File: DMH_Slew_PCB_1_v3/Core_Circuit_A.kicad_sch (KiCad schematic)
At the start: 60 parts, among them J1 TS_Jack_6.35mm_Sw, J11 Conn_02x03_Top_Bottom, J12 Conn_02x06_Top_Bottom, J13 Conn_02x03_Top_Bottom, J14 Conn_02x03_Top_Bottom, J15 Conn_02x06_Top_Bottom, J16 Conn_02x03_Top_Bottom, J17 Conn_01x08, J18 Conn_01x08, J19 Conn_01x08, J2 TS_Jack_6.35mm_Sw, J20 Conn_01x08, J3 TS_Jack_6.35mm_Sw, Q1 BC548, Q2 BC548, Q3 BC558, Q4 BC558, SW1 SW_DPDT_3way, SW2 SW_DPDT, SW3 SPDT_OnOffOn, U1 TL074, U2 TL074

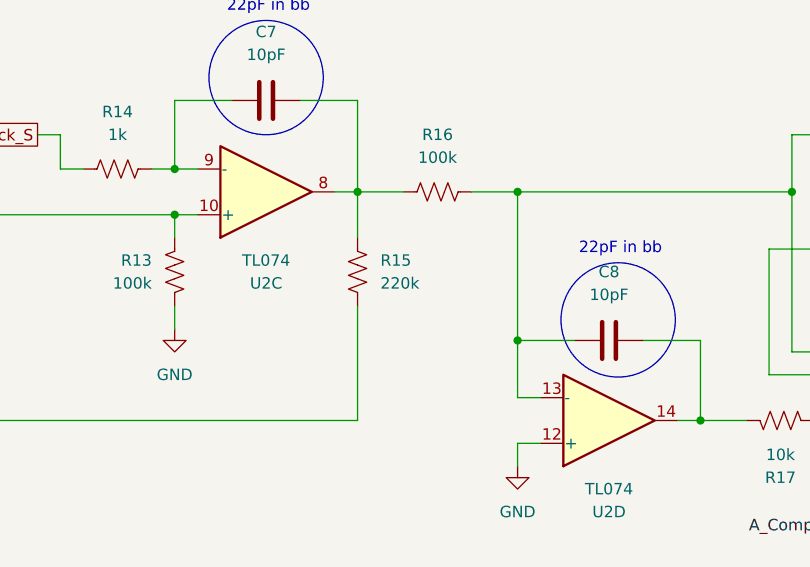
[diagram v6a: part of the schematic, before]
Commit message: Changed loopback resistor to 82k
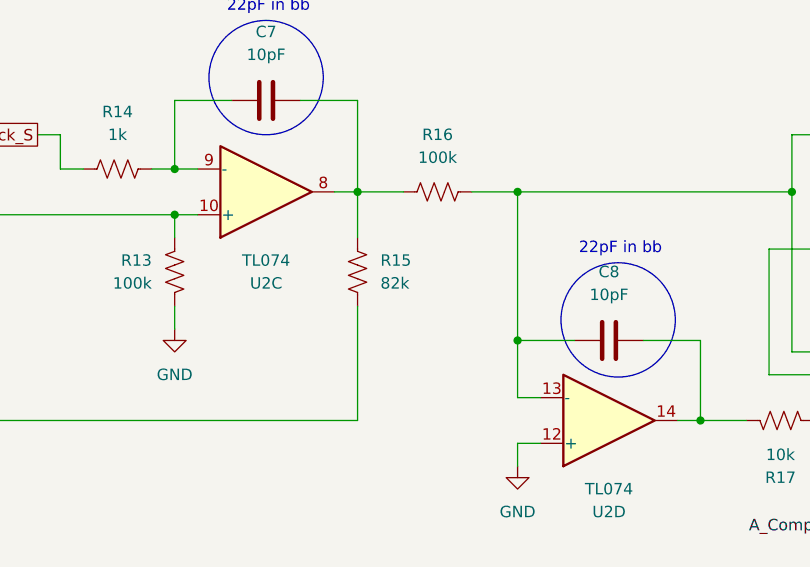
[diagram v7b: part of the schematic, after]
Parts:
- R15: value 220k -> 82k
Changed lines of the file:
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@@
 			)
 		)
-		(property "Value" "220k"
+		(property "Value" "82k"
 			(at 146.05 175.2599 0)
 			(effects

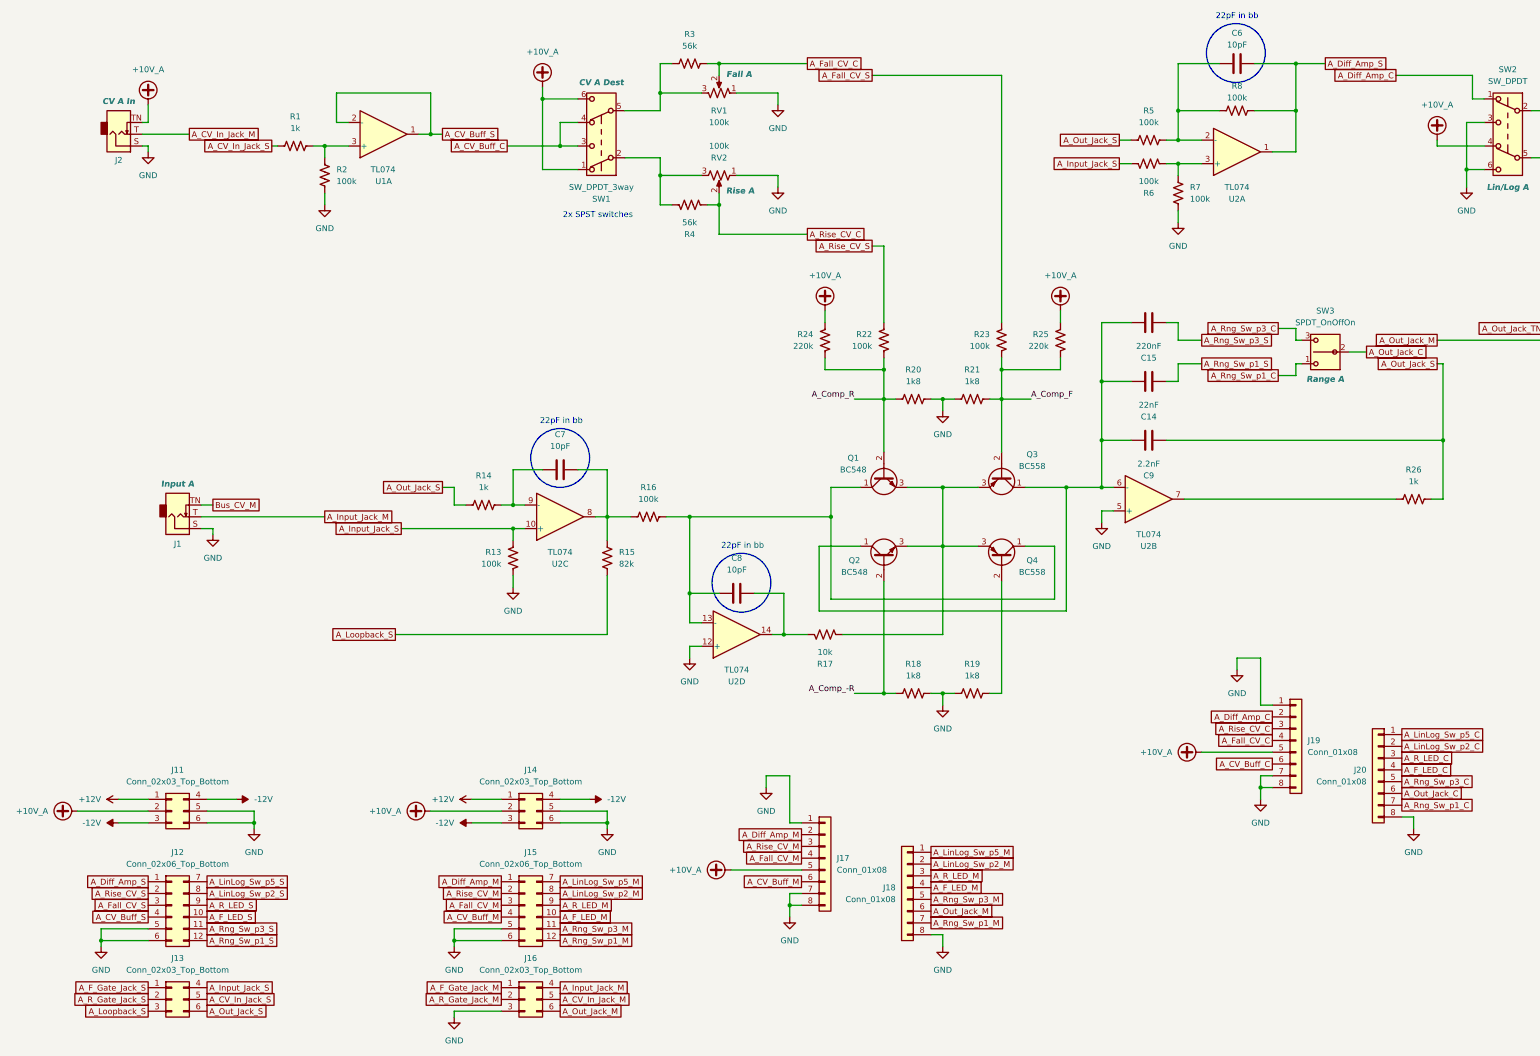
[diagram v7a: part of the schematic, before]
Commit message: Redesigned Main PCB
and regenerated Gerbers
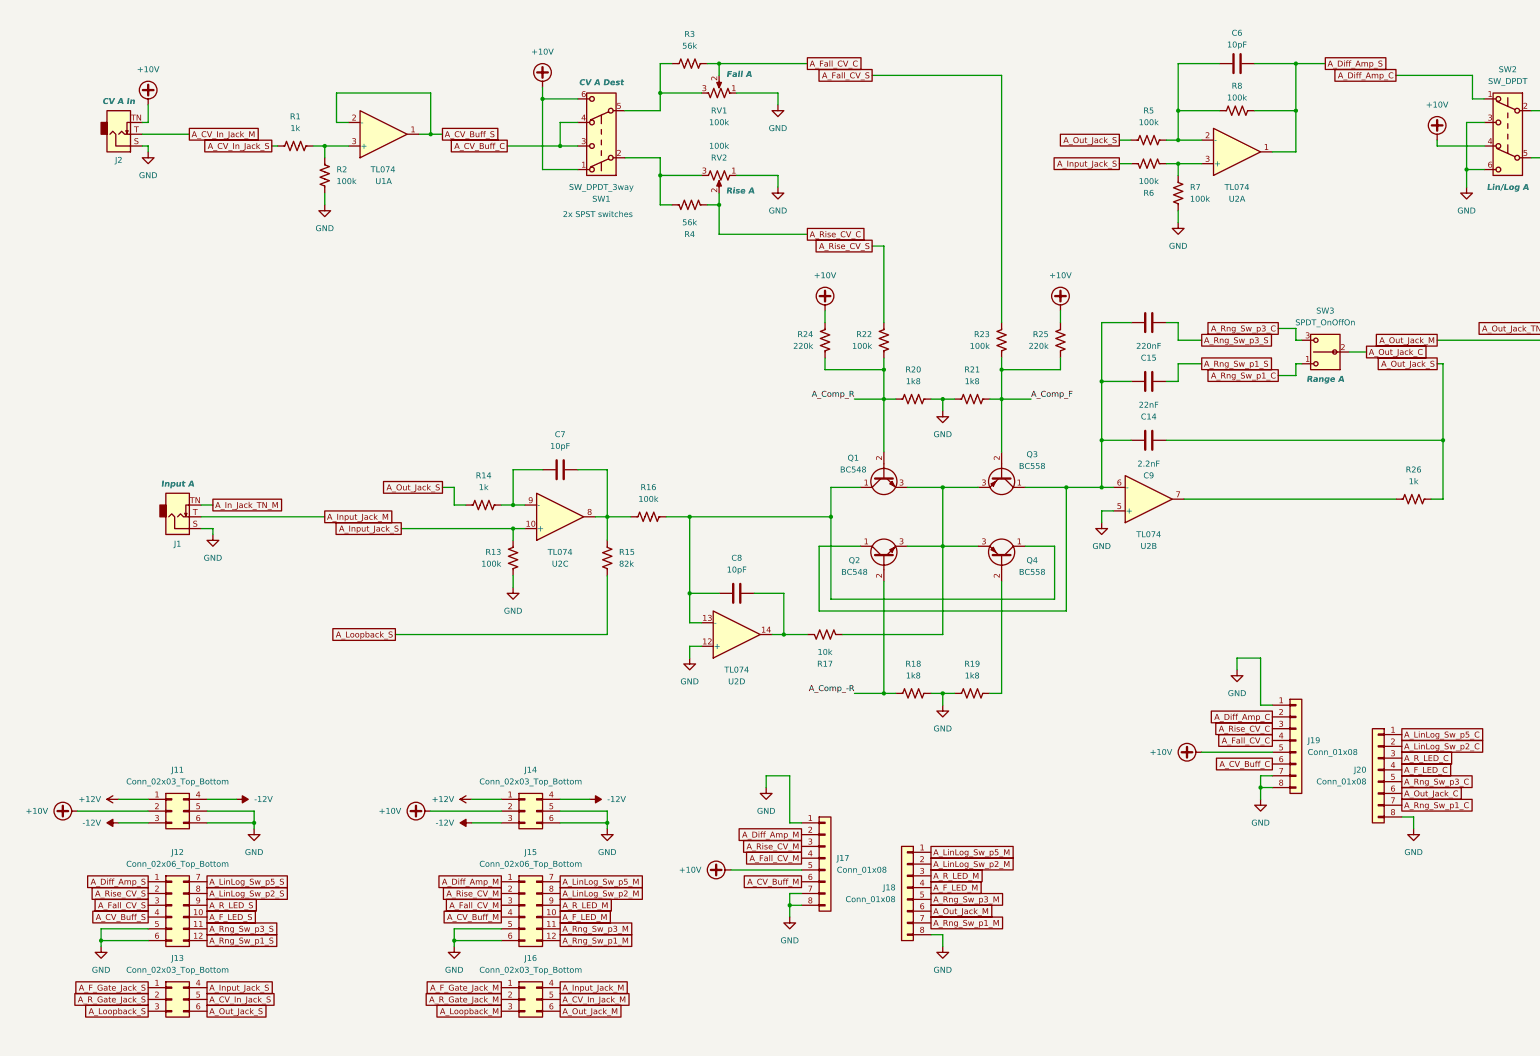
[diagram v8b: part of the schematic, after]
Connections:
- net GND: no longer J16.3 (Pin_3)
- net +10V_A renamed +10V
- net Bus_CV_M renamed A_In_Jack_TN_M
- new net A_Loopback_M: J16.3 (Pin_3)
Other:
- note removed: "22pF in bb"
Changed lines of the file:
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@@
 		(comment 1 "PCB for 5 cm Kosmo format synthesizer module")
 	)
-	(circle
-		(center 133.35 152.4)
-		(radius 6.35)
-		(stroke
-			(width 0)
-			(type default)
-		)
-		(fill
-			(type none)
-		)
-	)
-	(circle
-		(center 279.146 65.024)
-		(radius 6.35)
-		(stroke
-			(width 0)
-			(type default)
-		)
-		(fill
-			(type none)
-		)
-	)
-	(circle
-		(center 172.466 179.324)
-		(radius 6.35)
-		(stroke
-			(width 0)
-			(type default)
-		)
-		(fill
-			(type none)
-		)
-	)
-	(text "22pF in bb"
-		(exclude_from_sim no)
-		(at 133.604 144.526 0)
-		(effects
-			(font
-				(size 1.27 1.27)
-			)
-		)
-	)
-	(text "22pF in bb"
-		(exclude_from_sim no)
-		(at 279.4 57.15 0)
-		(effects
-			(font
-				(size 1.27 1.27)
-			)
-		)
-	)
 	(text "2x SPST switches"
 		(exclude_from_sim no)
@@
 		)
 	)
-	(text "22pF in bb"
-		(exclude_from_sim no)
-		(at 172.72 171.45 0)
-		(effects
-			(font
-				(size 1.27 1.27)
-			)
-		)
-	)
 	(junction
 		(at 215.9 139.7)
@@
 	(wire
 		(pts
-			(xy 120.65 271.78) (xy 110.49 271.78)
-		)
-		(stroke
-			(width 0)
-			(type default)
-		)
-	)
-	(wire
-		(pts
 			(xy 29.21 228.6) (xy 44.45 228.6)
 		)
@@
 	(wire
 		(pts
-			(xy 110.49 271.78) (xy 110.49 273.05)
-		)
-		(stroke
-			(width 0)
-			(type default)
-		)
-	)
-	(wire
-		(pts
 			(xy 384.81 68.58) (xy 393.7 68.58)
 		)
@@
 		)
 	)
-	(global_label "Bus_CV_M"
+	(global_label "A_In_Jack_TN_M"
 		(shape passive)
 		(at 58.42 162.56 0)
@@
 		)
 		(property "Intersheetrefs" "${INTERSHEET_REFS}"
-			(at 70.5975 162.56 0)
+			(at 74.9895 162.56 0)
 			(effects
 				(font
@@
 		)
 	)
+	(global_label "A_Loopback_M"
+		(shape passive)
+		(at 120.65 271.78 180)
+		(fields_autoplaced yes)
+		(effects
+			(font
+				(size 1.27 1.27)
+			)
+			(justify right)
+		)
+		(property "Intersheetrefs" "${INTERSHEET_REFS}"
+			(at 105.4111 271.78 0)
+			(effects
+				(font
+					(size 1.27 1.27)
+				)
+				(justify right)
+				(hide yes)
+			)
+		)
+	)
 	(global_label "A_Diff_Amp_M"
 		(shape passive)
@@
 			)
 		)
-		(property "Value" "+10V_A"
+		(property "Value" "+10V"
 			(at 322.58 76.2 0)
 			(effects
@@
 			)
 		)
-		(property "Value" "+10V_A"
+		(property "Value" "+10V"
 			(at 241.3 113.03 0)
 			(effects
@@
 			)
 		)
-		(property "Value" "+10V_A"
+		(property "Value" "+10V"
 			(at 265.43 215.8999 90)
 			(effects
@@
 			)
 		)
-		(property "Value" "+10V_A"
+		(property "Value" "+10V"
 			(at 129.54 64.77 0)
 			(effects
@@
 			)
 		)
-		(property "Value" "+10V_A"
+		(property "Value" "+10V"
 			(at 22.86 228.5999 90)
 			(effects
@@
 			)
 		)
-		(property "Value" "+10V_A"
+		(property "Value" "+10V"
 			(at 190.5 113.03 0)
 			(effects
@@
 			)
 		)
-		(property "Value" "+10V_A"
+		(property "Value" "+10V"
 			(at 163.83 241.2999 90)
 			(effects
@@
 			)
 		)
-		(property "Value" "+10V_A"
+		(property "Value" "+10V"
 			(at 44.45 68.58 0)
 			(effects
@@
 	)
 	(symbol
-		(lib_id "power:GND")
-		(at 110.49 273.05 0)
-		(unit 1)
-		(exclude_from_sim no)
-		(in_bom yes)
-		(on_board yes)
-		(dnp no)
-		(fields_autoplaced yes)
-		(property "Reference" "#PWR022"
-			(at 110.49 279.4 0)
-			(effects
-				(font
-					(size 1.27 1.27)
-				)
-				(hide yes)
-			)
-		)
-		(property "Value" "GND"
-			(at 110.49 278.13 0)
-			(effects
-				(font
-					(size 1.27 1.27)
-				)
-			)
-		)
-		(property "Footprint" ""
-			(at 110.49 273.05 0)
-			(effects
-				(font
-					(size 1.27 1.27)
-				)
-				(hide yes)
-			)
-		)
-		(property "Datasheet" ""
-			(at 110.49 273.05 0)
-			(effects
-				(font
-					(size 1.27 1.27)
-				)
-				(hide yes)
-			)
-		)
-		(property "Description" "Power symbol creates a global label with name \"GND\" , ground"
-			(at 110.49 273.05 0)
-			(effects
-				(font
-					(size 1.27 1.27)
-				)
-				(hide yes)
-			)
-		)
-		(pin "1"
-		)
-		(instances
-			(project ""
-				(path "/58f4306d-5387-4983-bb08-41a2313fd315/7ad2d702-dfb7-4d49-a82d-34430dd5948f"
-					(reference "#PWR022")
-					(unit 1)
-				)
-			)
-		)
-	)
-	(symbol
 		(lib_id "SynthStuff:TS_Jack_6.35mm_Sw")
 		(at 355.6 127 180)
@@
 			)
 		)
-		(property "Value" "+10V_A"
+		(property "Value" "+10V"
 			(at 99.06 228.5999 90)
 			(effects
